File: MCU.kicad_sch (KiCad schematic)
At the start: 18 parts, among them J4 SWD, SW1 Reset, U1 STM32L431CBTx, Y1 8M

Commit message: finished? power on sch
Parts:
- added D5: Heartbeat, LED_SMD:LED_0805_2012Metric, symbol Device:LED
- added J6: UART Breakout, Connector_PinHeader_2.54mm:PinHeader_1x02_P2.54mm_Vertical, symbol Connector:Conn_01x02_Pin
- added R14: 2.2K, Resistor_SMD:R_0805_2012Metric, symbol Device:R
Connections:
- net GND: now also D5.1 (K)
- net USART1_RX: now also J6.2 (Pin_2)
- net USART1_TX: now also J6.1 (Pin_1)
- net PA0: now reaches U1.10 (PA0)
- net PA0: now also R14.1
- new net: D5.2 (A), R14.2
- no-connect marks 28 -> 27
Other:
- removed sheet CAN
- note added: "CAN"
- note added: "General Purpose LED"
- note added: "SWD"
- note added: "UART"
- note removed: "Internal Connections"
- moved on the sheet: C15, C21, C22, J4, NT1, R19, R29, SW1, U1, Y1

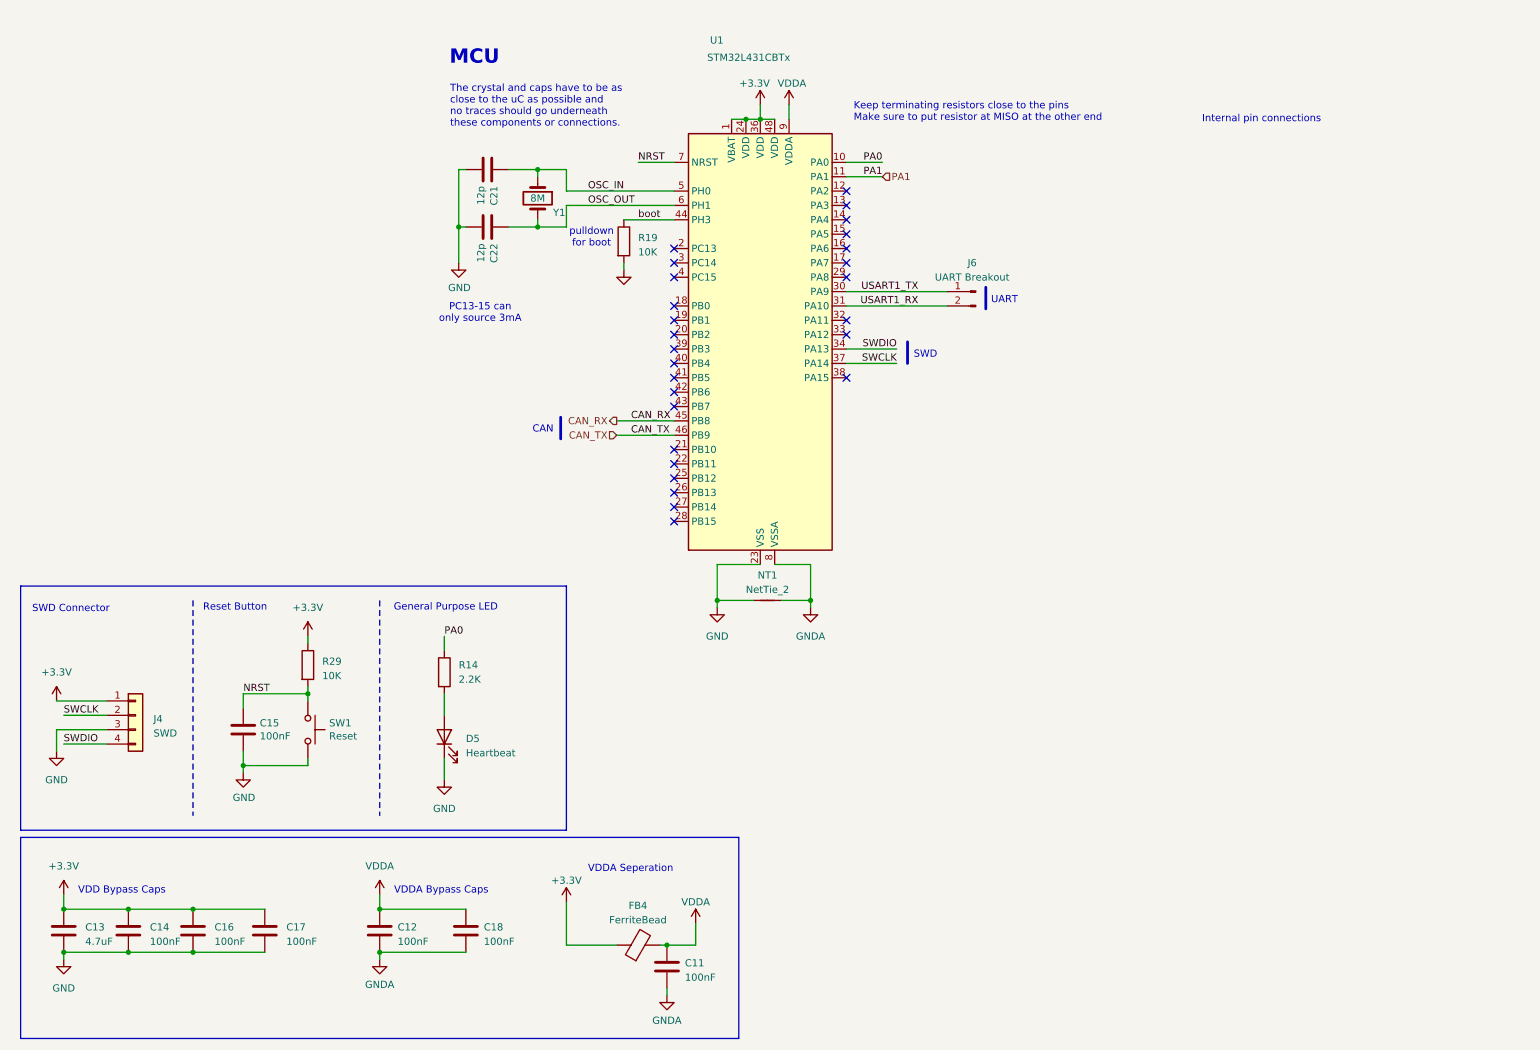
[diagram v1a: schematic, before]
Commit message: added MX cube pinout screenshot
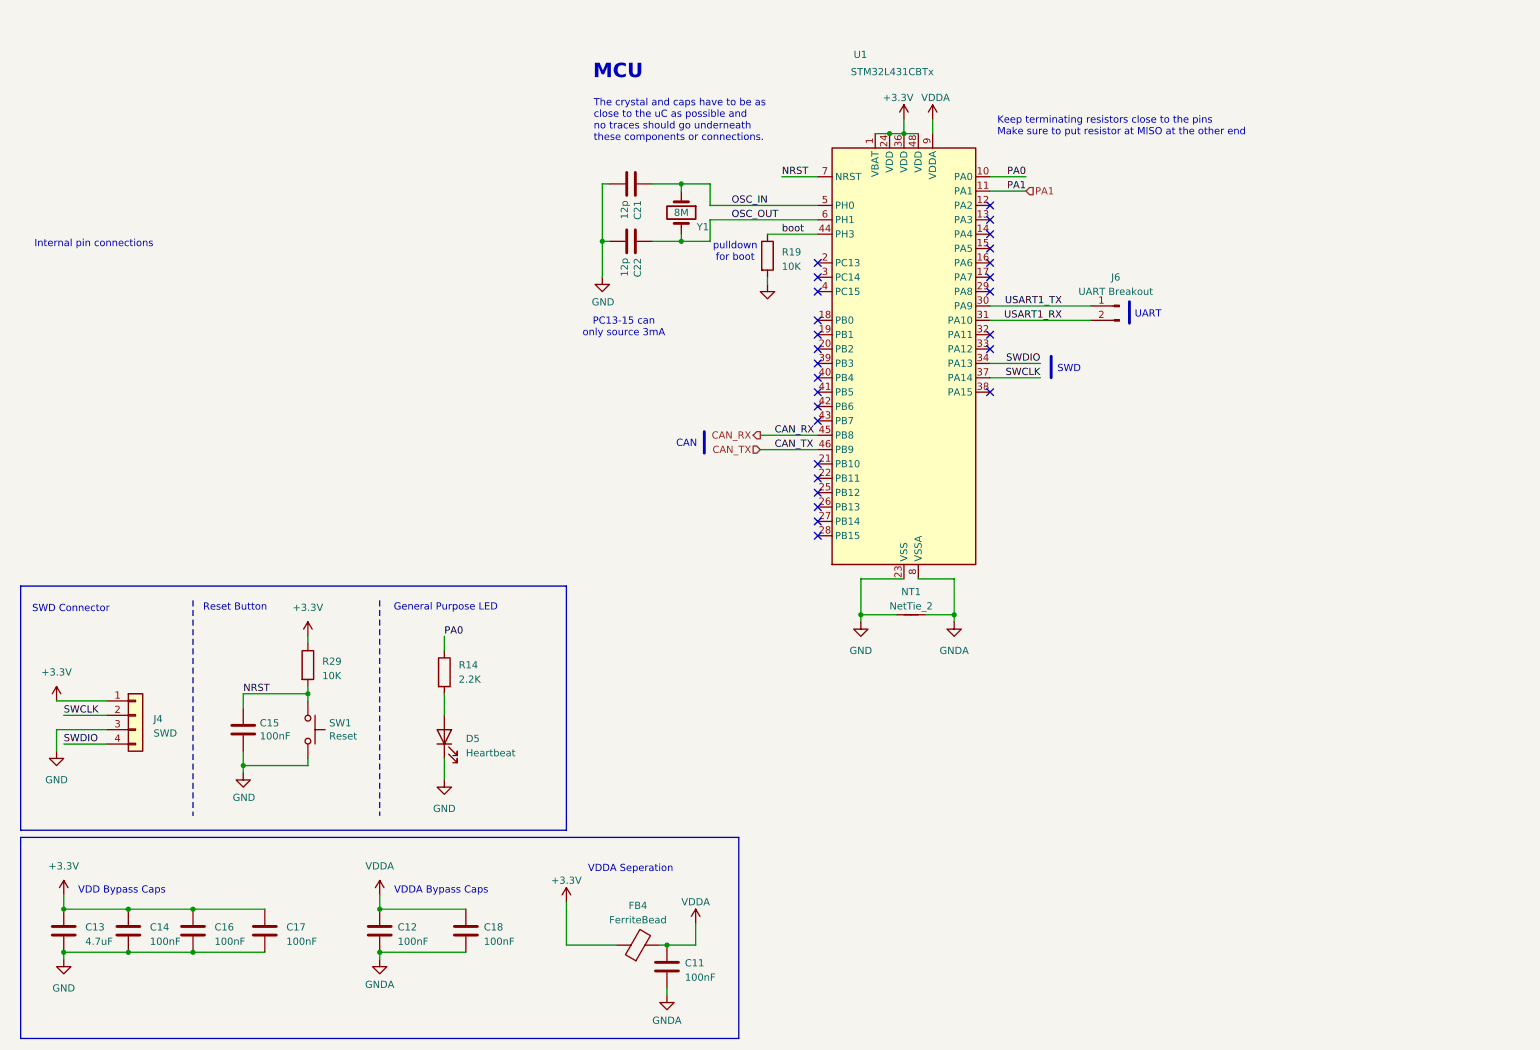
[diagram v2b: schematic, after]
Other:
- moved on the sheet: C21, C22, J6, NT1, R19, U1, Y1

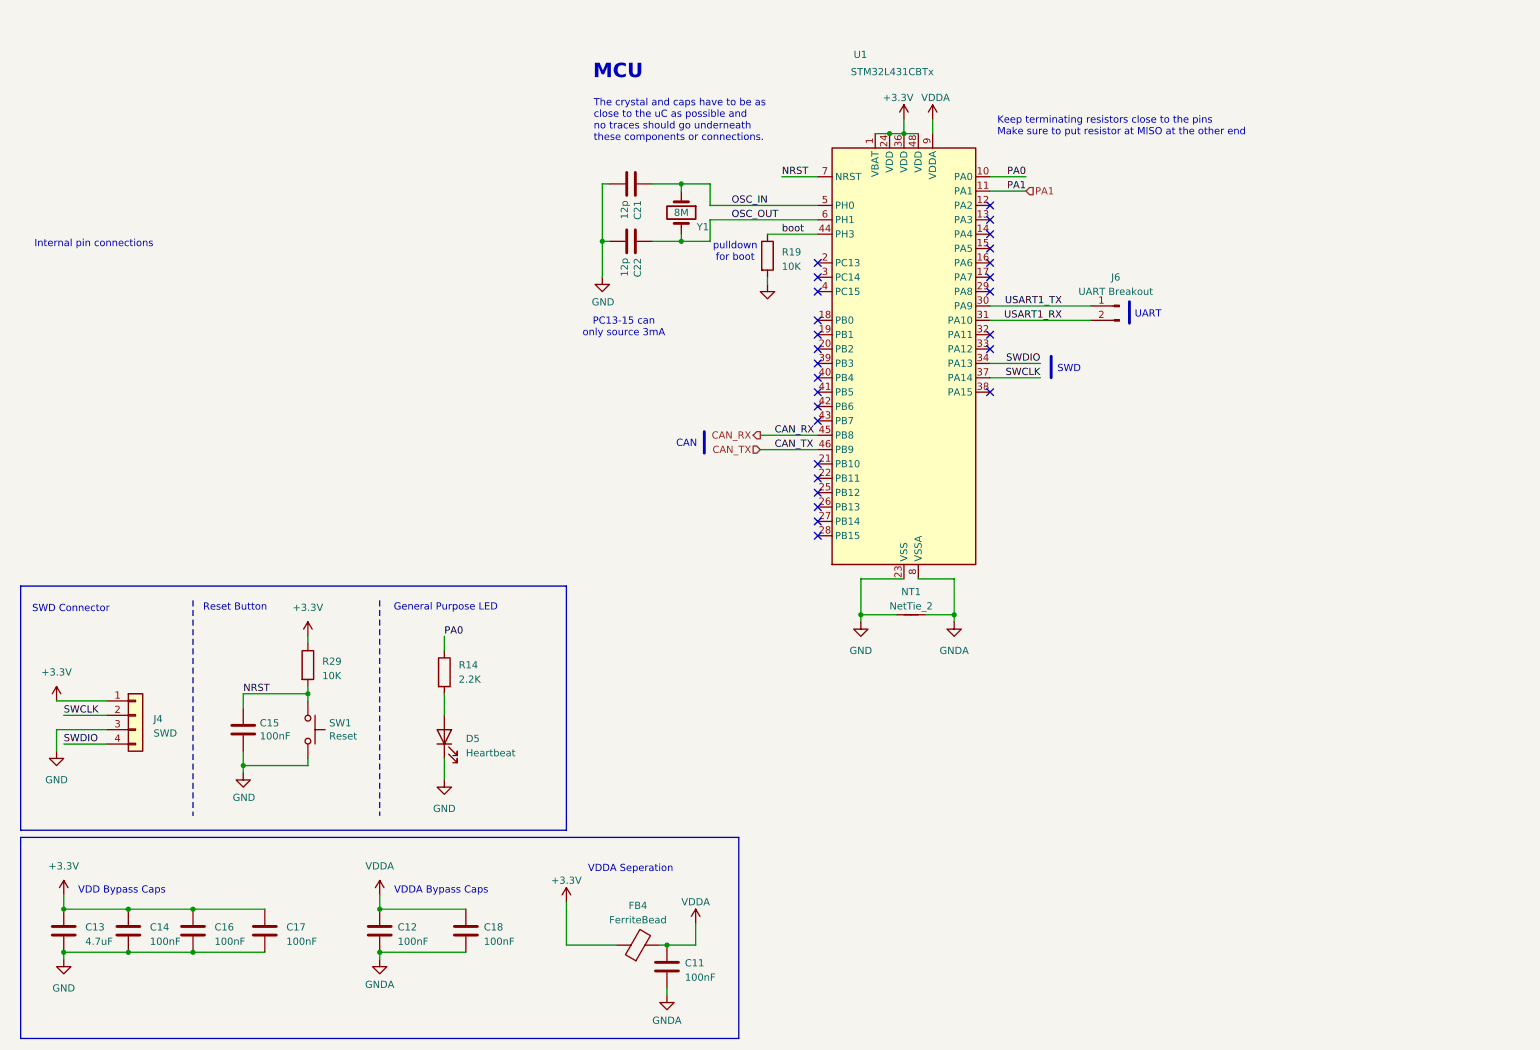
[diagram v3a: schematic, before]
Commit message: added 24V buck, bypass caps, more LEDs; started scrutineering circuit and bidirectional current sense
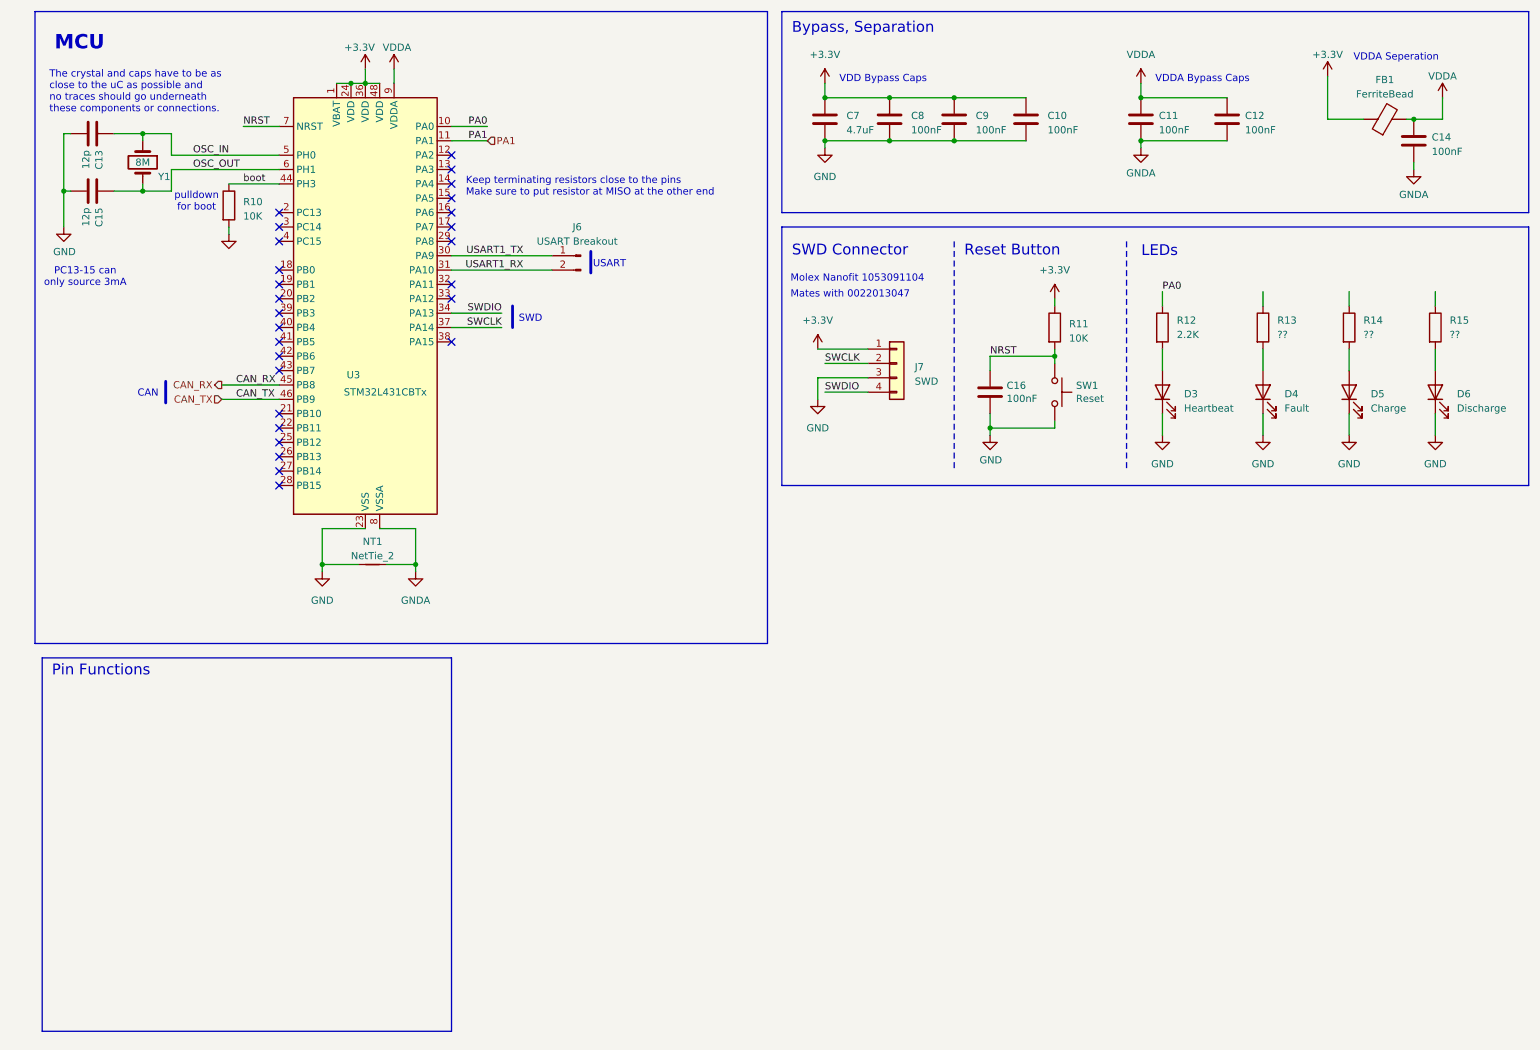
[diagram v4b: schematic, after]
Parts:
- removed J4: SWD, Connector_PinHeader_2.54mm:PinHeader_1x04_P2.54mm_Vertical, symbol Connector_Generic:Conn_01x04
- added D4: Fault, LED_SMD:LED_0805_2012Metric, symbol Device:LED
- added D5: Charge, LED_SMD:LED_0805_2012Metric, symbol Device:LED
- added D6: Discharge, LED_SMD:LED_0805_2012Metric, symbol Device:LED
- added J7: SWD, Connector_Molex:Molex_Nano-Fit_105309-xx04_1x04_P2.50mm_Vertical, symbol Connector_Generic:Conn_01x04
- added R13, R14, R15: ??, Resistor_SMD:R_0805_2012Metric, symbol Device:R
- J6: value UART Breakout -> USART Breakout
- renumbered C17 to C10, C12 to C11, C18 to C12, C21 to C13, C11 to C14, C22 to C15, C15 to C16, C13 to C7, C14 to C8, C16 to C9, D5 to D3, FB4 to FB1, R19 to R10, R29 to R11, R14 to R12, U1 to U3
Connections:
- net +3.3V: now also J7.1 (Pin_1)
- net GND: now also D4.1 (K), D5.1 (K), D6.1 (K), J7.3 (Pin_3)
- net SWCLK: now also J7.2 (Pin_2)
- net SWDIO: now also J7.4 (Pin_4)
- new net: D4.2 (A), R13.2
- new net: D5.2 (A), R14.2
- new net: D6.2 (A), R15.2
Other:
- note added: "Bypass, Separation"
- note added: "LEDs"
- note added: "Mates with 0022013047"
- note added: "Molex Nanofit 1053091104"
- note added: "Pin Functions"
- note added: "USART"
- note removed: "General Purpose LED"
- note removed: "Internal pin connections"
- note removed: "UART"
- moved on the sheet: C10, C11, C12, C13, C14, C15, C16, C7, C8, C9, D3, FB1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
